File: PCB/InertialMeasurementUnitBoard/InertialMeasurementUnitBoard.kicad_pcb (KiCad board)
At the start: 2 copper layers, 13 parts, among them U1 CD74HC4050PWR, X2 32.768 kHz

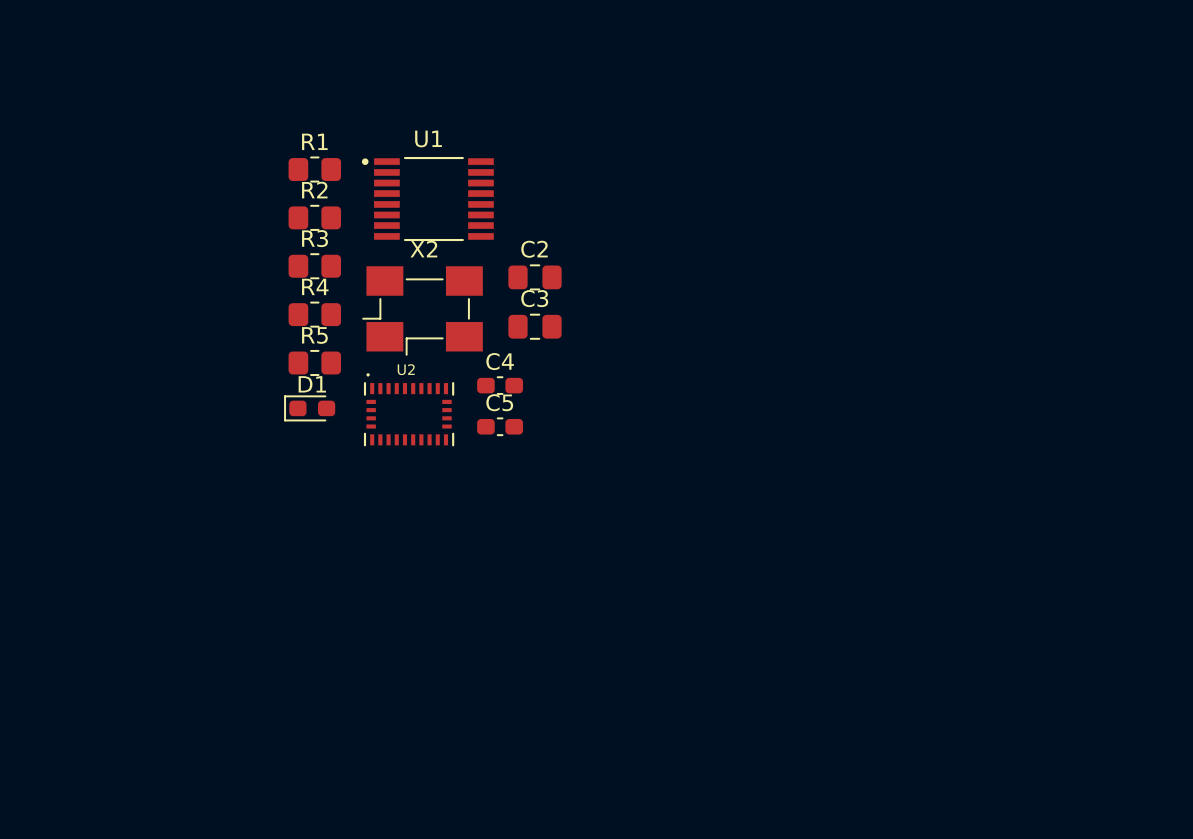
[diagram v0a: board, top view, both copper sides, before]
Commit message: 2/29 IMU Board
Added connectors to schematic, started layout
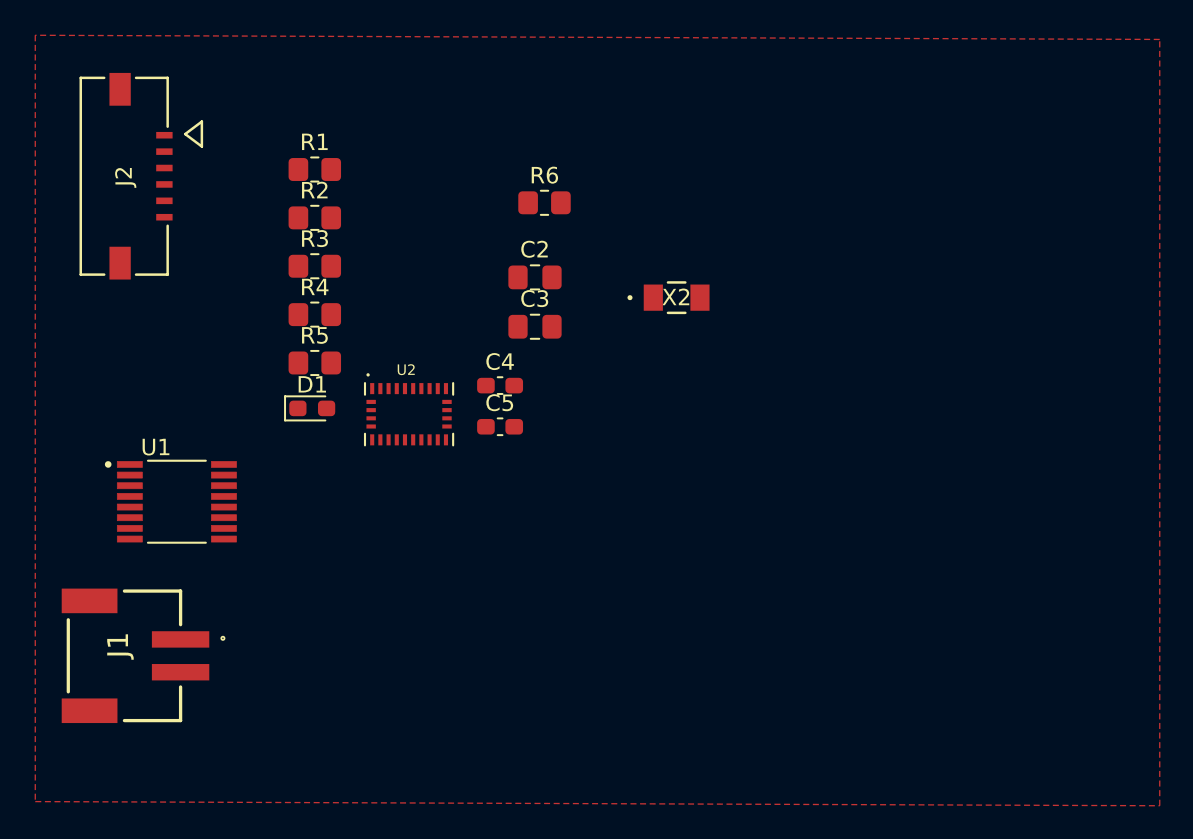
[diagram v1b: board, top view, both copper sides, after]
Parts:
- added J1: 1769, Adafruit Accessories JST-PH 2-pin SMT Right Angle Connect:1769, F.Cu at (105.4, 114.0)
- added J2: 2005280060, WM24188TR-ND:CON_2005280060_MOL, F.Cu at (101.9, 84.8)
- added R6: 10k, Resistor_SMD:R_0805_2012Metric_Pad1.20x1.40mm_HandSolder, F.Cu at (127.6, 86.4)
- X2: value 32.768 kHz -> SC32S-7PF20PPM; footprint Oscillator:Oscillator_SMD_Fordahl_DFAS15-4Pin_5.0x3.2mm_HandSoldering -> SC32S-7PF20PPM:XTAL_SC32S-7PF20PPM_EPS
- moved U1 24.2 mm to (105.2, 104.6)
- moved X2 15.4 mm to (135.6, 92.2)
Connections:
- R2 pad 2: Net-(U1-5A) -> /RST_N
- R3 pad 2: Net-(U1-4A) -> Net-(U1-3A)
- R5 pad 2: Net-(U1-3A) -> /CS_N
- U1 pad 10: /BOOT_N -> /RST_N_BUF
- U1 pad 11: Net-(U1-5A) -> +3.3V
- U1 pad 12: /RST_N -> /PS0_BUF
- U1 pad 15: /PS0/1 -> /PS1_BUF
- U1 pad 4: unconnected-(U1-2Y-Pad4) -> /CS_N_BUF
- U1 pad 5: unconnected-(U1-2A-Pad5) -> /CS_N
- U1 pad 6: /CS_N -> /BOOT_N_BUF
- U1 pad 9: Net-(U1-4A) -> /RST_N
- U2 pad 11: /RST_N -> /RST_N_BUF
- U2 pad 18: /CS_N -> /CS_N_BUF
- U2 pad 4: /BOOT_N -> /BOOT_N_BUF
- U2 pad 5: /PS0/1 -> /PS1_BUF
- U2 pad 6: /PS0/1 -> /PS0_BUF
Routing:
- added copper zone on F.Cu, net GND

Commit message: Recovery attempt 2
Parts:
- added GND1: TestPoint, TestPoint:TestPoint_THTPad_D2.0mm_Drill1.0mm, F.Cu at (101.1, 103.5)
- added H1: MountingHole, MountingHole:MountingHole_3.2mm_M3, F.Cu at (131.1, 80.0)
- added H2: MountingHole, MountingHole:MountingHole_3.2mm_M3, F.Cu at (131.1, 112.8)
- added H3: MountingHole, MountingHole:MountingHole_3.2mm_M3, F.Cu at (100.3, 112.8)
- added H4: MountingHole, MountingHole:MountingHole_3.2mm_M3, F.Cu at (100.3, 80.0)
- added VDD1: TestPoint, TestPoint:TestPoint_THTPad_D2.0mm_Drill1.0mm, F.Cu at (101.1, 98.7)
- moved J2 29.7 mm to (130.6, 92.5), turned to 90 degrees
- moved R6 26.9 mm to (108.4, 105.2), turned to -90 degrees
- moved J1 23.9 mm to (127.2, 104.4), turned to 90 degrees
- moved R3 21.2 mm to (120.5, 110.3), turned to 180 degrees
- moved R1 20.9 mm to (111.7, 105.2), turned to -90 degrees
- moved C3 20.3 mm to (107.5, 88.2), turned to 180 degrees
- moved C2 20.3 mm to (109.3, 81.1), turned to -90 degrees
- moved C5 19.0 mm to (125.2, 81.1), turned to -90 degrees
- moved X2 18.9 mm to (121.1, 80.1)
- moved C4 18.3 mm to (117.1, 81.0), turned to -90 degrees
- moved R2 17.8 mm to (120.5, 103.7), turned to 180 degrees
- moved R4 14.7 mm to (105.1, 105.2), turned to 90 degrees
- moved D1 13.5 mm to (105.1, 109.5), turned to 90 degrees
- moved R5 12.8 mm to (120.5, 107.0), turned to 180 degrees
- moved U2 12.4 mm to (115.9, 87.4)
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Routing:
- net +3.3V: track 0.00 -> 98.9 mm
- net /PS0_BUF: track 0.00 -> 38.4 mm
- net /PS1_BUF: track 0.00 -> 33.8 mm
- net /CS_N: track 0.00 -> 33.2 mm, vias 0 -> 2
- net /MOSI: track 0.00 -> 32.3 mm, vias 0 -> 2
- net /CS_N_BUF: track 0.00 -> 31.4 mm
- net /BOOT_N_BUF: track 0.00 -> 28.7 mm, vias 0 -> 2
- net GND: track 0.00 -> 24.1 mm, vias 0 -> 10
- net /MISO: track 0.00 -> 22.6 mm, vias 0 -> 2
- net /RST_N: track 0.00 -> 22.3 mm, vias 0 -> 2
- net /SCLK: track 0.00 -> 18.0 mm, vias 0 -> 2
- net /RST_N_BUF: track 0.00 -> 16.0 mm
- net Net-(U2-CLKSEL1/XOUT32): track 0.00 -> 15.4 mm
- net /INT_N: track 0.00 -> 13.9 mm, vias 0 -> 2
- net Net-(U1-3A): track 0.00 -> 13.3 mm
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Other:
- board outline added: 38.6 x 40.6 mm
- board text added: "PWR"

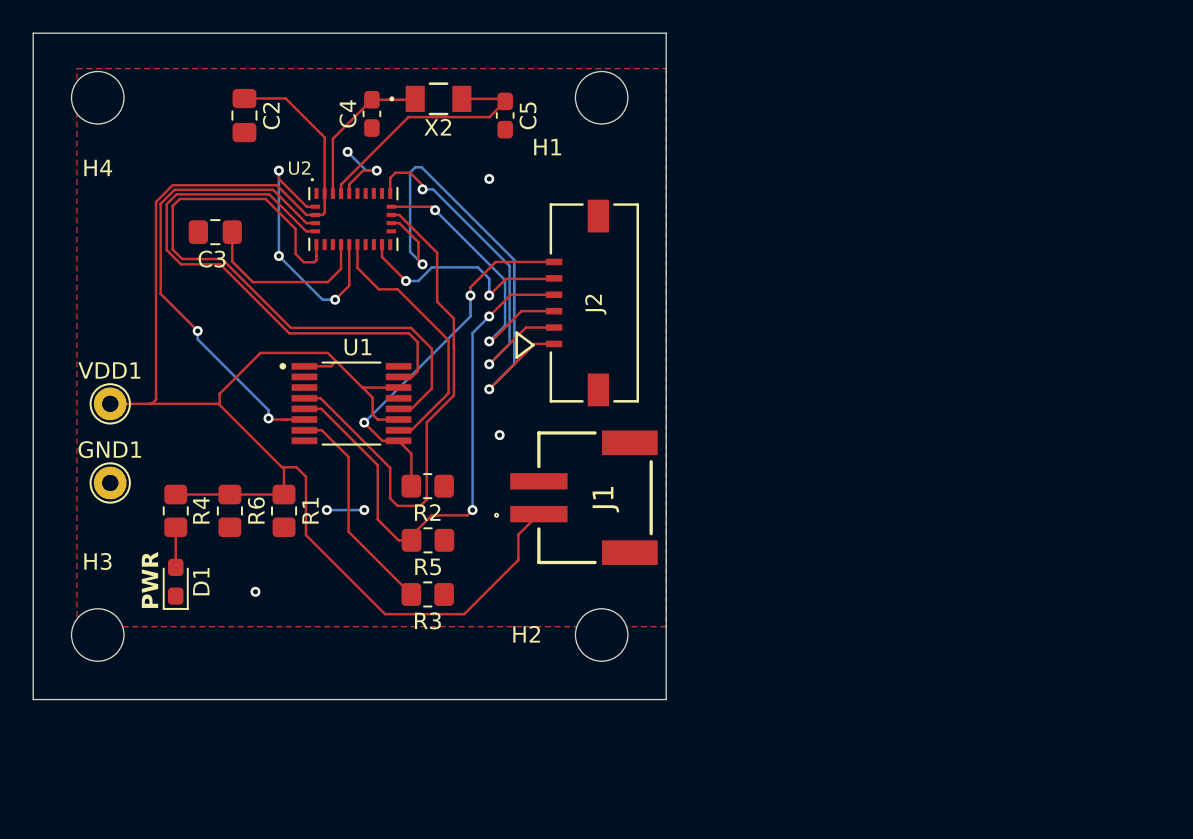
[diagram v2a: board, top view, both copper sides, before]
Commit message: Update IMU Board thicker power trace
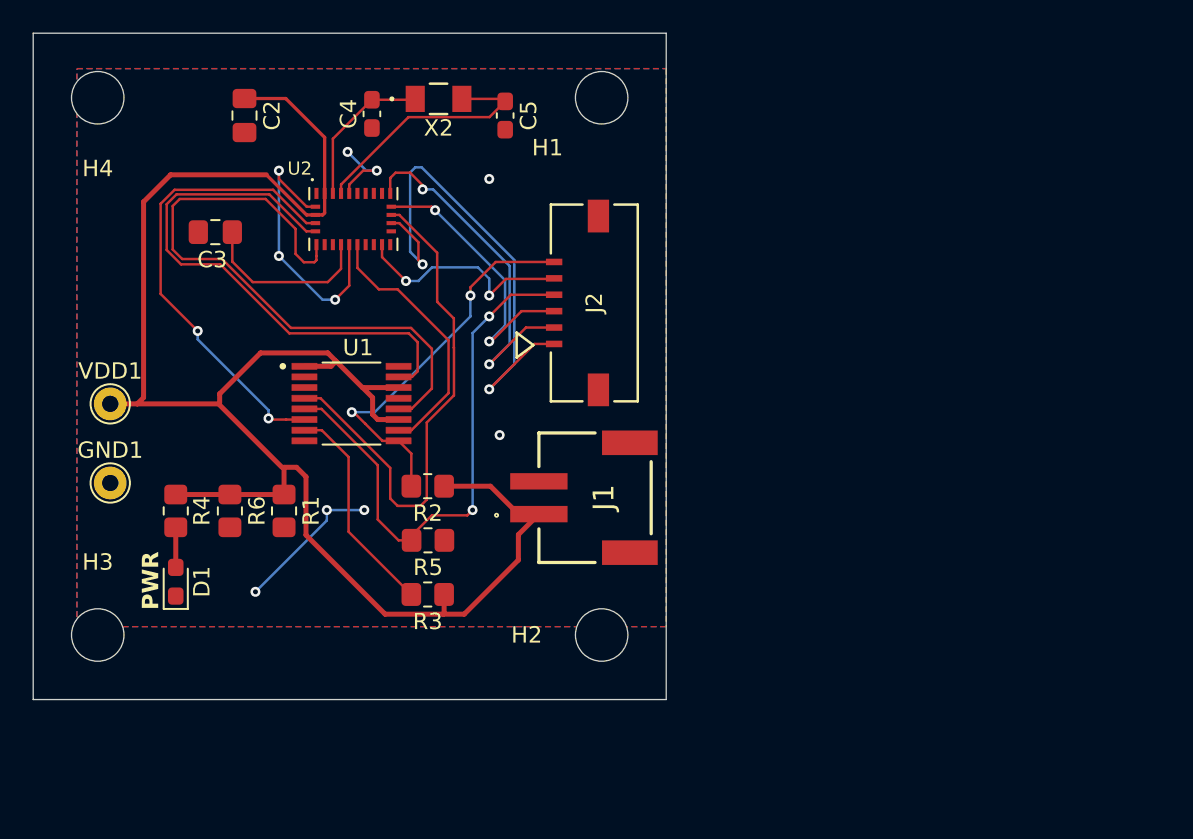
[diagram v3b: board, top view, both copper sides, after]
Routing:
- net +3.3V: track 98.9 -> 107.9 mm
- net GND: track 24.1 -> 30.9 mm
- net /RST_N: track 22.3 -> 23.8 mm
- added copper zone on B.Cu, net GND

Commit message: Update trace widths IMU
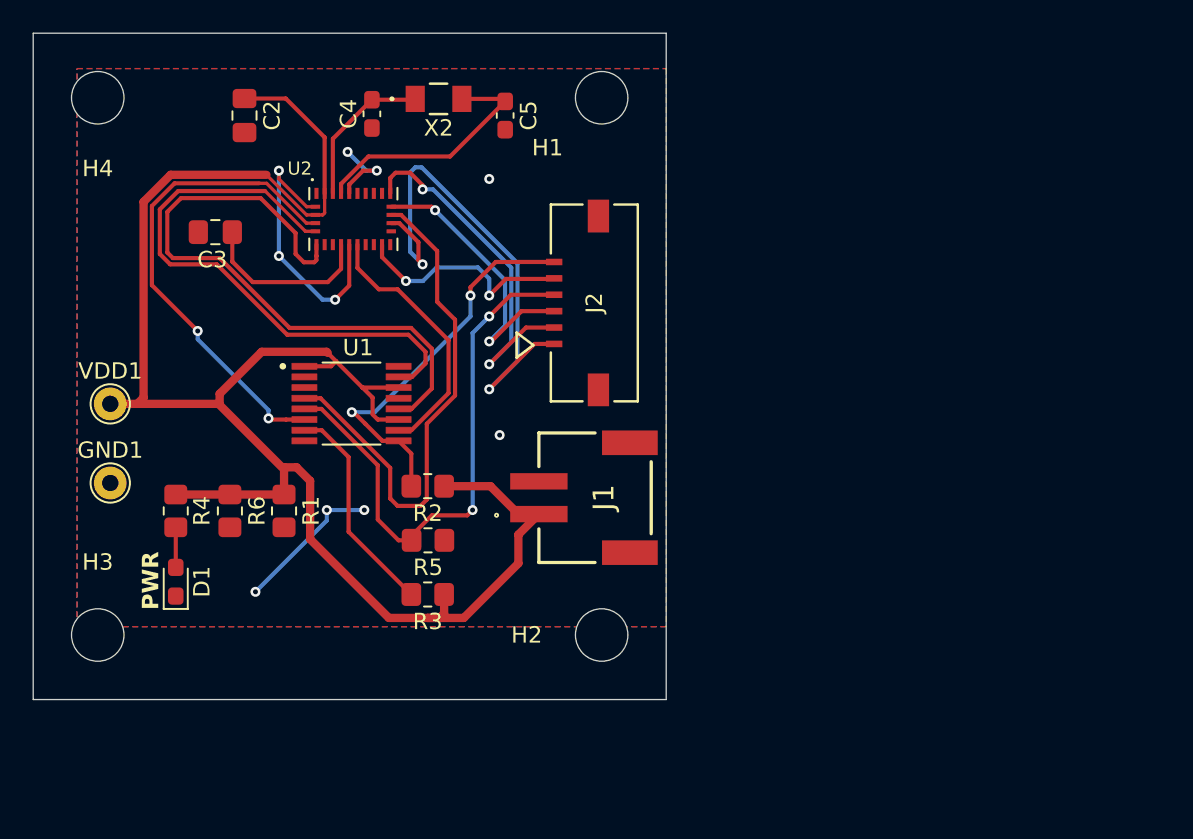
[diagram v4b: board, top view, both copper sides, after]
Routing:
- net +3.3V: track 107.9 -> 109.3 mm
- net /PS1_BUF: track 33.8 -> 35.1 mm
- net /BOOT_N_BUF: track 28.7 -> 29.7 mm

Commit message: Small updates on IMU, initial finish of MCU
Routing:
- net GND: track 30.9 -> 38.1 mm, vias 10 -> 11
- net +3.3V: track 109.3 -> 110.6 mm
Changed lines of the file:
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@@
+		(net 1)
+	)
+	(via
+		(at 104.8258 82.8548)
+		(size 0.61)
+		(drill 0.3)
+		(layers "F.Cu" "B.Cu")
 		(net 1)
 	)
@@
 	)
 	(segment
+		(start 106.426 84.455)
+		(end 104.8258 82.8548)
+		(width 0.254)
+		(layer "B.Cu")
+		(net 1)
+	)
+	(segment
 		(start 117.348 84.455)
 		(end 116.713 84.455)
@@
 	)
 	(segment
+		(start 111.379 84.455)
+		(end 106.426 84.455)
+		(width 0.254)
+		(layer "B.Cu")
+		(net 1)
+	)
+	(segment
 		(start 114.3 105.156)
 		(end 114.3 105.790169)
@@
 		(start 111.797 80.057)
 		(end 109.2785 80.057)
-		(width 0.254)
+		(width 0.508)
 		(layer "F.Cu")
 		(net 2)
@@
 	)
 	(segment
+		(start 114.1685 85.8435)
+		(end 114.1685 84.3489)
+		(width 0.254)
+		(layer "F.Cu")
+		(net 2)
+	)
+	(segment
 		(start 114.8665 96.0805)
 		(end 114.5605 96.3865)
@@
 	)
 	(segment
+		(start 112.0394 82.2198)
+		(end 112.0394 80.2994)
+		(width 0.508)
+		(layer "F.Cu")
+		(net 2)
+	)
+	(segment
 		(start 116.5275 97.6865)
 		(end 118.6765 97.6865)
@@
 	)
 	(segment
+		(start 110.617 83.6422)
+		(end 112.0394 82.2198)
+		(width 0.508)
+		(layer "F.Cu")
+		(net 2)
+	)
+	(segment
 		(start 104.775 84.709)
 		(end 110.617 84.709)
@@
 	)
 	(segment
-		(start 114.1685 87.0334)
-		(end 114.1685 85.8435)
-		(width 0.2032)
-		(layer "F.Cu")
-		(net 2)
-	)
-	(segment
 		(start 127.234 105.404)
 		(end 125.984 106.654)
@@
 	)
 	(segment
+		(start 112.0394 80.2994)
+		(end 111.797 80.057)
+		(width 0.508)
+		(layer "F.Cu")
+		(net 2)
+	)
+	(segment
 		(start 124.2805 103.7005)
 		(end 125.984 105.404)
@@
 	)
 	(segment
+		(start 114.1685 84.3489)
+		(end 113.8428 84.0232)
+		(width 0.254)
+		(layer "F.Cu")
+		(net 2)
+	)
+	(segment
 		(start 125.984 105.404)
 		(end 127.234 105.404)
@@
 	)
 	(segment
-		(start 114.0459 87.156)
-		(end 114.1685 87.0334)
-		(width 0.2032)
+		(start 112.0394 82.2198)
+		(end 113.8428 84.0232)
+		(width 0.508)
 		(layer "F.Cu")
 		(net 2)
@@
 		(start 122.6566 111.7346)
 		(end 120.4468 111.7346)
+		(width 0.508)
+		(layer "F.Cu")
+		(net 2)
+	)
+	(segment
+		(start 110.617 84.709)
+		(end 110.617 83.6422)
 		(width 0.508)
 		(layer "F.Cu")
@@
 	)
 	(segment
-		(start 114.1685 85.8435)
-		(end 114.1685 82.4285)
-		(width 0.254)
-		(layer "F.Cu")
-		(net 2)
-	)
-	(segment
 		(start 103.124 98.298)
 		(end 103.124 86.36)
 		(width 0.508)
-		(layer "F.Cu")
-		(net 2)
-	)
-	(segment
-		(start 114.1685 82.4285)
-		(end 111.797 80.057)
-		(width 0.254)
 		(layer "F.Cu")
 		(net 2)
@@
 		(layer "F.Cu")
 		(net 2)
-	)
-	(segment
-		(start 113.606 87.156)
-		(end 114.0459 87.156)
-		(width 0.2032)
-		(layer "F.Cu")
-		(net 2)
